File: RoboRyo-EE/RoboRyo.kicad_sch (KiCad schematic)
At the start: 13 parts, among them IC2 LD29080DT33R, IC3 LD29080DT50R, Q1 DMG9926USD-13, U1 STM32F446RETx, U2 ATmega328P-MM

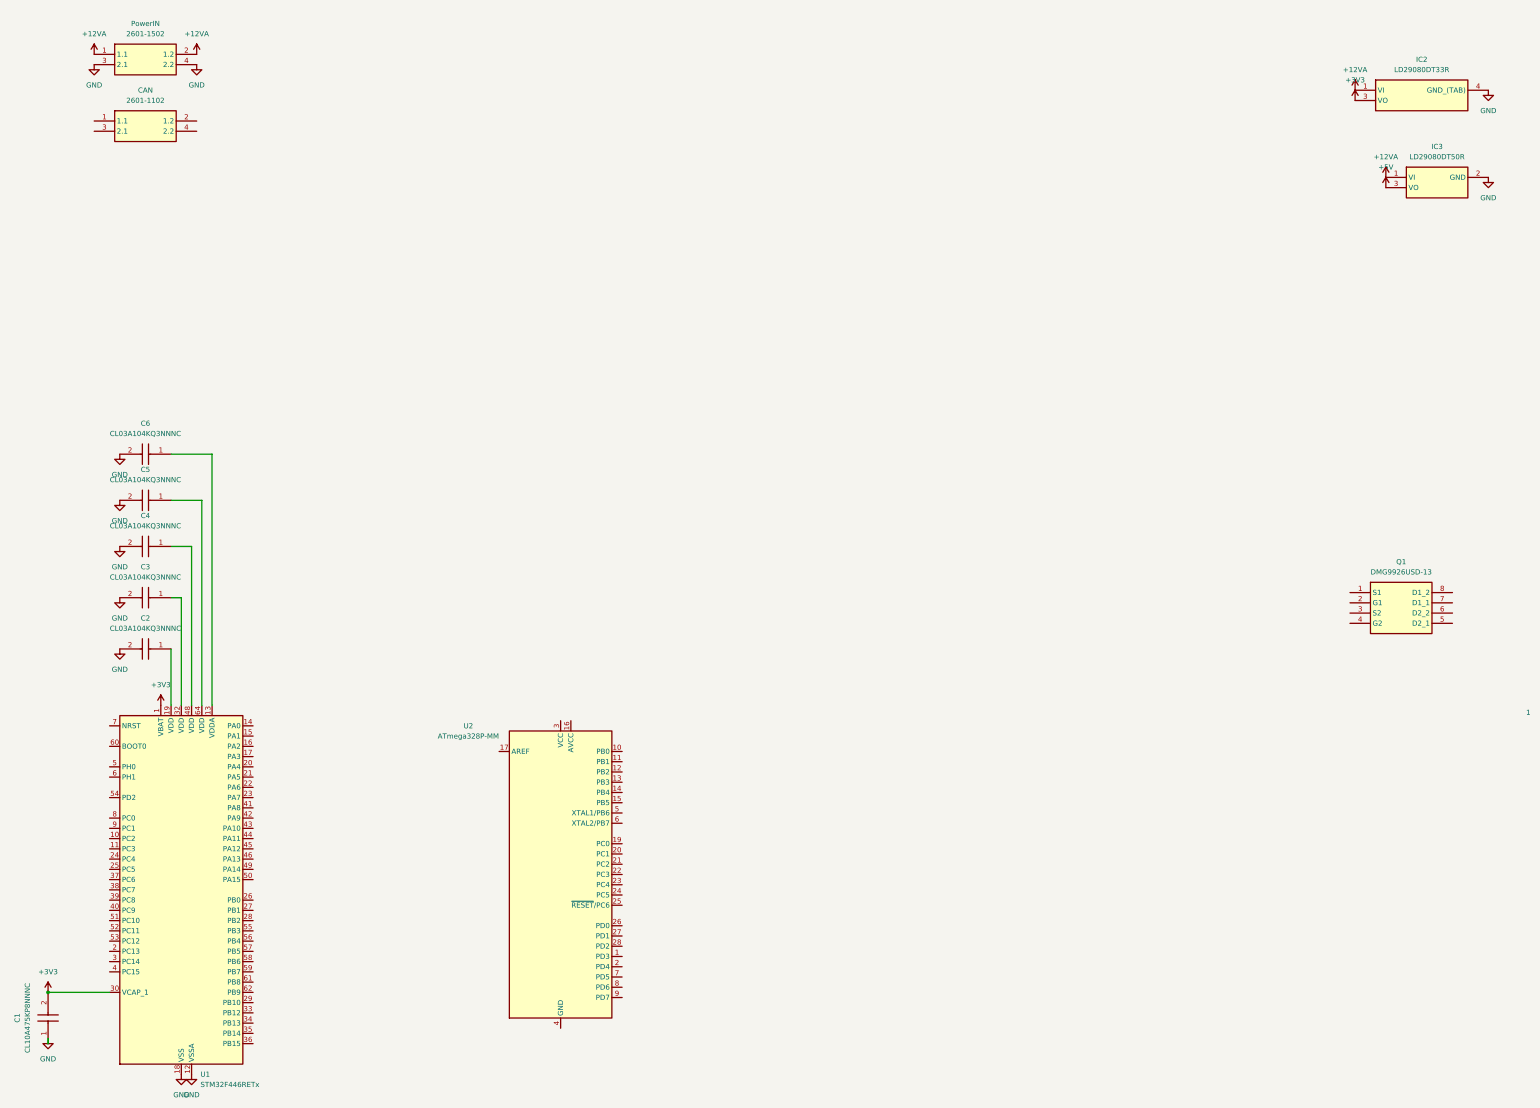
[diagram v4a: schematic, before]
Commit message: added diodes and the PCB is now solonoid ready
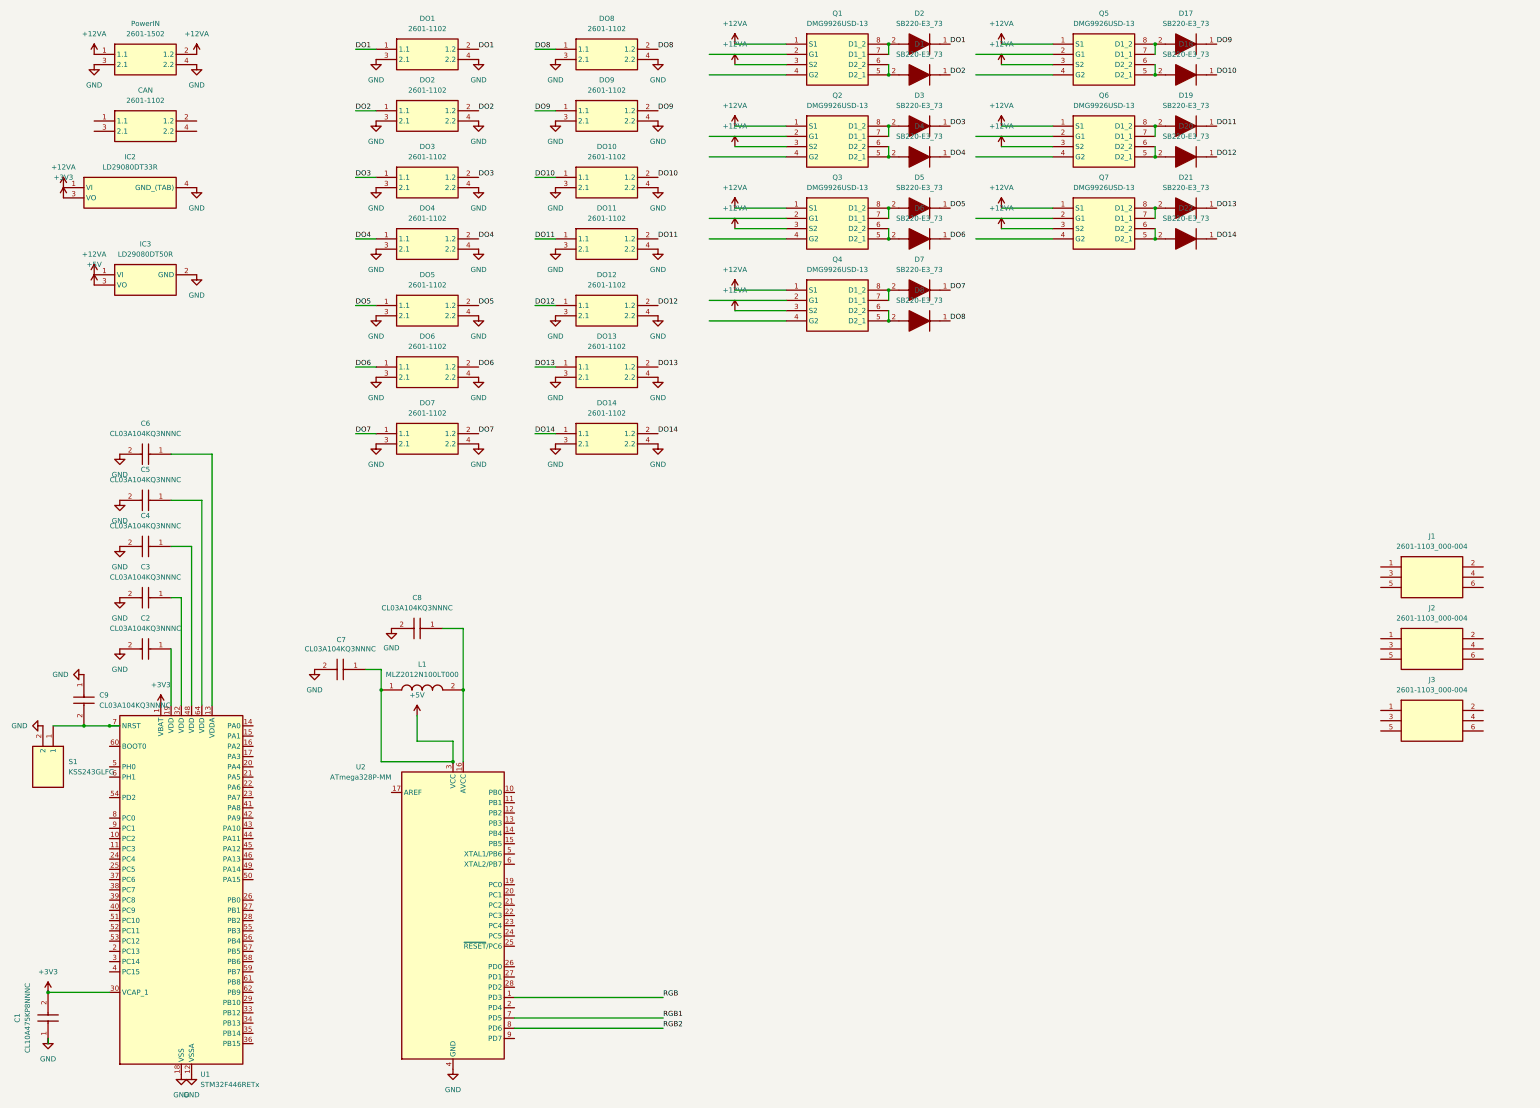
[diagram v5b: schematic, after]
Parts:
- added C7, C8, C9: CL03A104KQ3NNNC, CAPC0603X33N, symbol SamacSys_Parts:CL03A104KQ3NNNC
- added D1, D17, D18, D19, D2, D20, D21, D22, D3, D4, D5, D6, D7, D8: SB220-E3_73, DIOAD1910W86L670D310, symbol SamacSys_Parts:SB220-E3_73
- added DO1, DO10, DO11, DO12, DO13, DO14, DO2, DO3, DO4, DO5, DO6, DO7, DO8, DO9: 2601-1102, 26011102, symbol SamacSys_Parts:2601-1102
- added J1, J2, J3: 2601-1103_000-004, 26011103, symbol SamacSys_Parts:2601-1103_000-004
- added L1: MLZ2012N100LT000, INDC2012X105N, symbol SamacSys_Parts:MLZ2012N100LT000
- added Q2, Q3, Q4, Q5, Q6, Q7: DMG9926USD-13, SOIC127P600X175-8N, symbol SamacSys_Parts:DMG9926USD-13
- added S1: KSS243GLFG, KSS, symbol SamacSys_Parts:KSS243GLFG
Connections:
- net +12VA: now also Q1.1 (S1), Q1.3 (S2), Q2.1 (S1), Q2.3 (S2), Q3.1 (S1), Q3.3 (S2), Q4.1 (S1), Q4.3 (S2), Q5.1 (S1), Q5.3 (S2), Q6.1 (S1), Q6.3 (S2), Q7.1 (S1), Q7.3 (S2)
- net +5V: now also U2.3 (VCC), C7.1, L1.1
- net GND: now also U2.18 (GND), U2.29 (GND), U2.4 (GND), C7.2, C8.2, C9.1, DO1.3 (2.1), DO1.4 (2.2), DO10.3 (2.1), DO10.4 (2.2), DO11.3 (2.1), DO11.4 (2.2), DO12.3 (2.1), DO12.4 (2.2), DO13.3 (2.1), DO13.4 (2.2), DO14.3 (2.1), DO14.4 (2.2), DO2.3 (2.1), DO2.4 (2.2), DO3.3 (2.1), DO3.4 (2.2), DO4.3 (2.1), DO4.4 (2.2), DO5.3 (2.1), DO5.4 (2.2), DO6.3 (2.1), DO6.4 (2.2), DO7.3 (2.1), DO7.4 (2.2), DO8.3 (2.1), DO8.4 (2.2), DO9.3 (2.1), DO9.4 (2.2), S1.2
- net RGB: now reaches U2.1 (PD3)
- net at U2.16 (AVCC): now also C8.1, L1.2
- net RGB1: now reaches U2.7 (PD5)
- net RGB2: now reaches U2.8 (PD6)
- net at Q1.5 (D2_1): now also Q1.6 (D2_2), D1.2 (A)
- net at Q1.7 (D1_1): now also Q1.8 (D1_2), D2.2 (A)
- net at U1.7 (NRST): now also C9.2, S1.1
- new net: D8.2 (A), Q4.5 (D2_1), Q4.6 (D2_2)
- new net: D7.2 (A), Q4.7 (D1_1), Q4.8 (D1_2)
- new net: D6.2 (A), Q3.5 (D2_1), Q3.6 (D2_2)
- new net: D3.2 (A), Q2.7 (D1_1), Q2.8 (D1_2)
- new net: D5.2 (A), Q3.7 (D1_1), Q3.8 (D1_2)
- new net: D20.2 (A), Q6.5 (D2_1), Q6.6 (D2_2)
- new net: D19.2 (A), Q6.7 (D1_1), Q6.8 (D1_2)
- new net: D17.2 (A), Q5.7 (D1_1), Q5.8 (D1_2)
- new net: D21.2 (A), Q7.7 (D1_1), Q7.8 (D1_2)
- new net: D18.2 (A), Q5.5 (D2_1), Q5.6 (D2_2)
- new net: D4.2 (A), Q2.5 (D2_1), Q2.6 (D2_2)
- new net: D22.2 (A), Q7.5 (D2_1), Q7.6 (D2_2)
- new net DO1: D2.1 (K), DO1.1 (1.1), DO1.2 (1.2)
- new net DO10: D18.1 (K), DO10.1 (1.1), DO10.2 (1.2)
- new net DO11: D19.1 (K), DO11.1 (1.1), DO11.2 (1.2)
- new net DO12: D20.1 (K), DO12.1 (1.1), DO12.2 (1.2)
- new net DO13: D21.1 (K), DO13.1 (1.1), DO13.2 (1.2)
- new net DO14: D22.1 (K), DO14.1 (1.1), DO14.2 (1.2)
- new net DO2: D1.1 (K), DO2.1 (1.1), DO2.2 (1.2)
- new net DO3: D3.1 (K), DO3.1 (1.1), DO3.2 (1.2)
- new net DO4: D4.1 (K), DO4.1 (1.1), DO4.2 (1.2)
- new net DO5: D5.1 (K), DO5.1 (1.1), DO5.2 (1.2)
- new net DO6: D6.1 (K), DO6.1 (1.1), DO6.2 (1.2)
- new net DO7: D7.1 (K), DO7.1 (1.1), DO7.2 (1.2)
- new net DO8: D8.1 (K), DO8.1 (1.1), DO8.2 (1.2)
- new net DO9: D17.1 (K), DO9.1 (1.1), DO9.2 (1.2)
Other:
- note removed: "1"
- moved on the sheet: IC2, IC3, Q1, U2

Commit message: added connector ports for PWM
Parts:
- removed D21, D22: SB220-E3_73, DIOAD1910W86L670D310, symbol SamacSys_Parts:SB220-E3_73
- removed DO13, DO14: 2601-1102, 26011102, symbol SamacSys_Parts:2601-1102
- removed Q7: DMG9926USD-13, SOIC127P600X175-8N, symbol SamacSys_Parts:DMG9926USD-13
- added C10, C11, C12, C13, C14: CL03A104KQ3NNNC, CAPC0603X33N, symbol SamacSys_Parts:CL03A104KQ3NNNC
- added C15: CL10A475KP8NNNC, CAPC1608X90N, symbol SamacSys_Parts:CL10A475KP8NNNC
- added IC1: CH552G, SOIC127P600X180-16N, symbol SamacSys_Parts:CH552G
- added J4, J5, J6, J7, J8: 2601-1103_000-004, 26011103, symbol SamacSys_Parts:2601-1103_000-004
- added S2: KSS243GLFG, KSS, symbol SamacSys_Parts:KSS243GLFG
- added Y1: ABM3-16.000MHZ-D2Y-T, ABM3, symbol SamacSys_Parts:ABM3-16.000MHZ-D2Y-T
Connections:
- net +3V3: now also C13.2, IC1.16 (V33)
- net +5V: now also J1.3 (2.1), J1.4 (2.2), J2.3 (2.1), J2.4 (2.2), J3.3 (2.1), J3.4 (2.2), C15.1, J4.3 (2.1), J4.4 (2.2), J5.3 (2.1), J5.4 (2.2), J6.3 (2.1), J6.4 (2.2), J7.3 (2.1), J7.4 (2.2), J8.3 (2.1), J8.4 (2.2)
- net GND: now also J1.5 (3.1), J1.6 (3.2), J2.5 (3.1), J2.6 (3.2), J3.5 (3.1), J3.6 (3.2), C10.1, C11.1, C12.1, C13.1, C14.1, C15.2, IC1.14 (GND/VSS), J4.5 (3.1), J4.6 (3.2), J5.5 (3.1), J5.6 (3.2), J6.5 (3.1), J6.6 (3.2), J7.5 (3.1), J7.6 (3.2), J8.5 (3.1), J8.6 (3.2), S2.1
- net at U2.17 (AREF): now also C12.2
- net RST: now reaches U2.25 (~{RESET}/PC6)
- net RST: now also IC1.2 (P1.4/T2_/CAP1_/SCS/TIN2/UCC1/AIN1), S2.2
- net at U2.5 (XTAL1/PB6): now also C10.2, Y1.2
- net at U2.6 (XTAL2/PB7): now also C11.2, Y1.1
- net at J3.1 (1.1): now also J3.2 (1.2)
- net A-IN4: now reaches U1.10 (PC2)
- net A-IN5: now reaches U1.11 (PC3)
- net mPWM6: now reaches U1.14 (PA0)
- net mPWM5: now reaches U1.15 (PA1)
- net mPWM4: now reaches U1.16 (PA2)
- net mPWM3: now reaches U1.17 (PA3)
- net JTAG-WKUP: now reaches U1.2 (PC13)
- net GPIO-IN6: now reaches U1.20 (PA4)
- net SPI_CLK: now reaches U1.21 (PA5)
- net SPI_MISO: now reaches U1.22 (PA6)
- net A-IN1: now reaches U1.23 (PA7)
- net GPIO-OUT10: now reaches U1.24 (PC4)
- net GPIO-OUT8: now reaches U1.25 (PC5)
- net GPIO-OUT9: now reaches U1.26 (PB0)
- net GPIO-OUT2: now reaches U1.27 (PB1)
- net mPWM2: now reaches U1.28 (PB2)
- net mPWM1: now reaches U1.29 (PB10)
- net GPIO-OUT14: now reaches U1.3 (PC14)
- net CAN_RX: now reaches U1.33 (PB12)
- net CAN_RX: now also CAN.1 (1.1), CAN.2 (1.2)
- net CAN_TX: now reaches U1.34 (PB13)
- net CAN_TX: now also CAN.3 (2.1), CAN.4 (2.2)
- net GPIO-OUT6: now reaches U1.35 (PB14)
- net GPIO-OUT7: now reaches U1.36 (PB15)
- net GPIO-OUT5: now reaches U1.37 (PC6)
- net GPIO-OUT4: now reaches U1.38 (PC7)
- net GPIO-OUT3: now reaches U1.39 (PC8)
- net GPIO-OUT13: now reaches U1.4 (PC15)
- net GPIO-OUT1: now reaches U1.40 (PC9)
- net GPIO-IN5: now reaches U1.41 (PA8)
- net GPIO-IN4: now reaches U1.42 (PA9)
- net GPIO-IN3: now reaches U1.43 (PA10)
- net GPIO-IN2: now reaches U1.44 (PA11)
- net GPIO-IN1: now reaches U1.45 (PA12)
- net JTAG-SWDIO: now reaches U1.46 (PA13)
- net JTAG-CK-SWCLK: now reaches U1.49 (PA14)
- net GPIO-OUT12: now reaches U1.5 (PH0)
- net JTAG-DI: now reaches U1.50 (PA15)
- net UART_RX: now reaches U1.51 (PC10)
- net UART_TX: now reaches U1.52 (PC11)
- net GPIO-OUT15: now reaches U1.53 (PC12)
- net GPIO-OUT16: now reaches U1.54 (PD2)
- net JTAG-DO_SWO: now reaches U1.55 (PB3)
- net JTAG-RST: now reaches U1.56 (PB4)
- net SPI_MOSI: now reaches U1.57 (PB5)
- net I2C_SCL: now reaches U1.58 (PB6)
- net I2C_SDA: now reaches U1.59 (PB7)
- net GPIO-OUT11: now reaches U1.6 (PH1)
- net mPWM8: now reaches U1.61 (PB8)
- net mPWM7: now reaches U1.62 (PB9)
- net A-IN2: now reaches U1.8 (PC0)
- net A-IN3: now reaches U1.9 (PC1)
- net at J2.1 (1.1): now also J2.2 (1.2)
- net at J1.1 (1.1): now also J1.2 (1.2)
- new net: J8.1 (1.1), J8.2 (1.2)
- new net: J5.1 (1.1), J5.2 (1.2)
- new net: C14.2, IC1.15 (VCC/VDD)
- new net: J6.1 (1.1), J6.2 (1.2)
- new net: J4.1 (1.1), J4.2 (1.2)
- new net: J7.1 (1.1), J7.2 (1.2)
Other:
- moved on the sheet: C1, C2, C3, C4, C5, C6, C7, C8, C9, D17, D18, D19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

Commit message: deleted critical power budget vunerability
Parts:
- removed C13, C14: CL03A104KQ3NNNC, CAPC0603X33N, symbol SamacSys_Parts:CL03A104KQ3NNNC
- removed D19, D20: SB220-E3_73, DIOAD1910W86L670D310, symbol SamacSys_Parts:SB220-E3_73
- removed DO11, DO12: 2601-1102, 26011102, symbol SamacSys_Parts:2601-1102
- removed IC1: CH552G, SOIC127P600X180-16N, symbol SamacSys_Parts:CH552G
- removed Q6: DMG9926USD-13, SOIC127P600X175-8N, symbol SamacSys_Parts:DMG9926USD-13
- removed S2: KSS243GLFG, KSS, symbol SamacSys_Parts:KSS243GLFG
- added D10, D11, D12, D13, D14, D15, D16, D9: CD1408-FF11500, DIOC3419X135N, symbol SamacSys_Parts:CD1408-FF11500
- added LED1-A: 150060AS75000, LEDC1608X80N, symbol SamacSys_Parts:150060AS75000
- added LED1-B: 150060BS75000, LEDC1608X80N, symbol SamacSys_Parts:150060BS75000
- added LED1-G: 150060GS75000, LEDC1608X80N, symbol SamacSys_Parts:150060GS75000
- added LED1-R: 150060RS75000, LEDC1608X80N, symbol SamacSys_Parts:150060RS75000
- added LED1-Y: 150060YS75000, LEDC1608X80N, symbol SamacSys_Parts:150060YS75000
- added R1: ERJ3GEYJ102V, ERJ3EKF1000V, symbol SamacSys_Parts:ERJ3GEYJ102V
- added RSL: APHHS1005SECK, APHHS1005SECK, symbol SamacSys_Parts:APHHS1005SECK
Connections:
- net at J8.1 (1.1), J8.2 (1.2): now also D16.1 (K)
- net at J5.1 (1.1), J5.2 (1.2): now also D10.1 (K)
- net at J3.1 (1.1), J3.2 (1.2): now also D13.1 (K)
- net at J6.1 (1.1), J6.2 (1.2): now also D12.1 (K)
- net at J4.1 (1.1), J4.2 (1.2): now also D15.1 (K)
- net at J2.1 (1.1), J2.2 (1.2): now also D11.1 (K)
- net at J1.1 (1.1), J1.2 (1.2): now also D9.1 (K)
- net at J7.1 (1.1), J7.2 (1.2): now also D14.1 (K)
- net GPIO-OUT2 renamed RSL_OUT
- new net ATMEGA-RX: R1.1

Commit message: Added a RSL for safety :nerd:
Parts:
- added D19, D20: SB220-E3_73, DIOAD1910W86L670D310, symbol SamacSys_Parts:SB220-E3_73
- added DO11, DO12, DO13: 2601-1102, 26011102, symbol SamacSys_Parts:2601-1102
- added Q6: DMG9926USD-13, SOIC127P600X175-8N, symbol SamacSys_Parts:DMG9926USD-13
- added Q7: CSD13383F4, CSD13383F4, symbol SamacSys_Parts:CSD13383F4
- added R2: ERJ3GEYJ102V, ERJ3EKF1000V, symbol SamacSys_Parts:ERJ3GEYJ102V
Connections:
- net +12VA: now also Q6.1 (S1), Q6.3 (S2)
- net +5V: now also Q7.2 (S)
- net DO10: now also D20.1 (K)
- net DO9: now also D19.1 (K)
- net GND: now also DO11.3 (2.1), DO11.4 (2.2), DO12.3 (2.1), DO12.4 (2.2), DO13.3 (2.1), DO13.4 (2.2)
- net RSL_OUT: now also R2.1
- net at RSL.1 (K): now also Q7.1 (G)
- net at RSL.2 (A): now also R2.2
- net GPIO-OUT9 renamed sRADIO_LED
- new net: D20.2 (A), Q6.5 (D2_1), Q6.6 (D2_2)
- new net: D19.2 (A), Q6.7 (D1_1), Q6.8 (D1_2)
- new net RSL_EX: DO13.1 (1.1), DO13.2 (1.2), Q7.3 (D)
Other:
- moved on the sheet: RSL
